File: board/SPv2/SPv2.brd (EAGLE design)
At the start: 63.8 x 22.9 mm, 33 parts, among them IC1 S34ML0XG1, IC2 F5508, IC4 74LS14D, Q1 12MHz

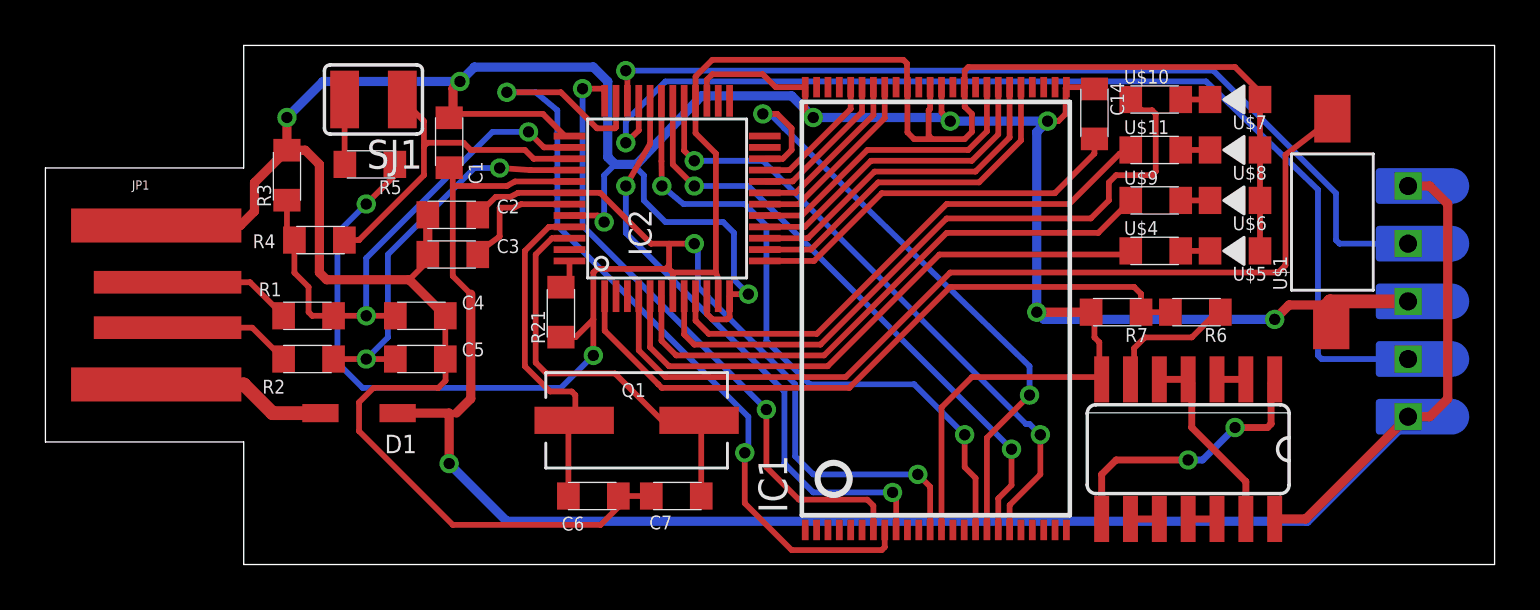
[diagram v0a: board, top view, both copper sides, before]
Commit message: added fiducals
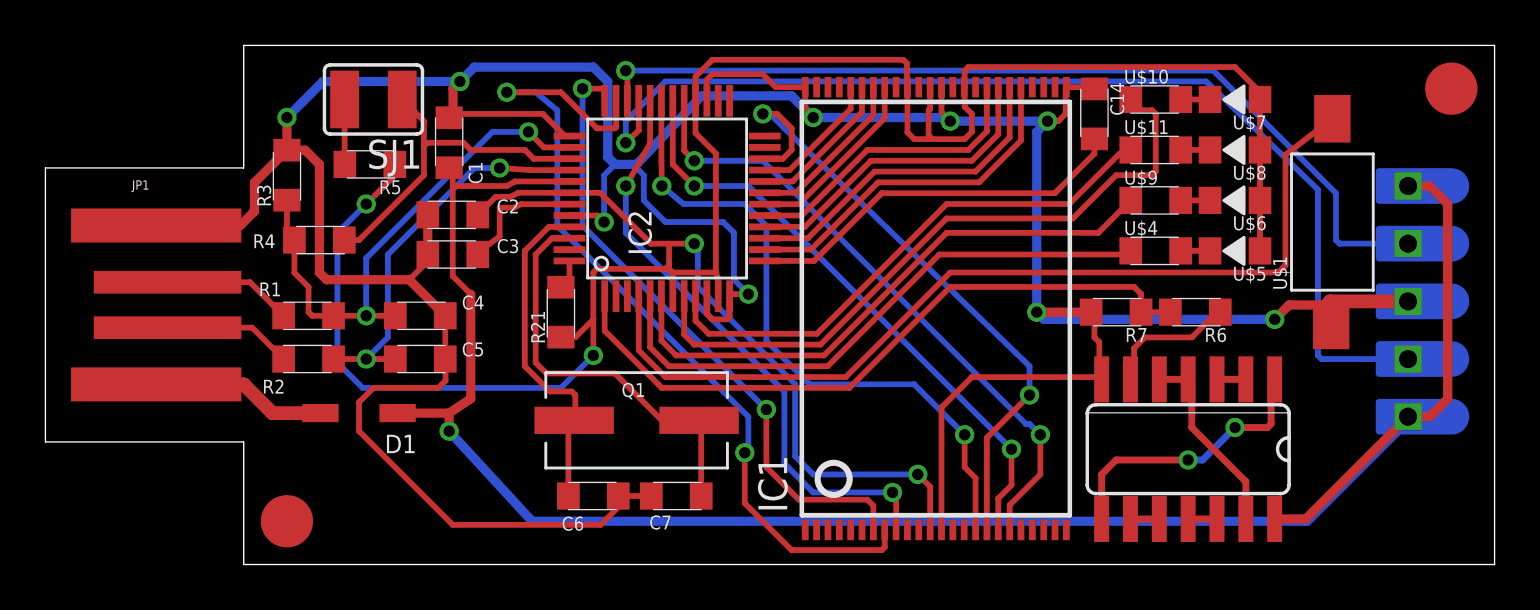
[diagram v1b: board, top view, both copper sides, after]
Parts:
- added U$12, U$3: FIDUCAL, Passives:FIDUCAL
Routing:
- net VBUS: track 87.3 -> 86.5 mm
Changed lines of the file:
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@@
 <grid distance="0.00625" unitdist="inch" unit="inch" style="lines" multiple="1" display="yes" altdistance="0.00625" altunitdist="inch" altunit="inch"/>
 <layers>
-<layer number="1" name="Top" color="4" fill="1" visible="no" active="yes"/>
+<layer number="1" name="Top" color="4" fill="1" visible="yes" active="yes"/>
 <layer number="2" name="Route2" color="1" fill="3" visible="no" active="no"/>
 <layer number="3" name="Route3" color="4" fill="3" visible="no" active="no"/>
@@
 <layer number="14" name="Route14" color="1" fill="6" visible="no" active="no"/>
 <layer number="15" name="Route15" color="4" fill="6" visible="no" active="no"/>
-<layer number="16" name="Bottom" color="1" fill="1" visible="no" active="yes"/>
-<layer number="17" name="Pads" color="2" fill="1" visible="no" active="yes"/>
-<layer number="18" name="Vias" color="2" fill="1" visible="no" active="yes"/>
+<layer number="16" name="Bottom" color="1" fill="1" visible="yes" active="yes"/>
+<layer number="17" name="Pads" color="2" fill="1" visible="yes" active="yes"/>
+<layer number="18" name="Vias" color="2" fill="1" visible="yes" active="yes"/>
 <layer number="19" name="Unrouted" color="6" fill="1" visible="yes" active="yes"/>
 <layer number="20" name="Dimension" color="15" fill="1" visible="yes" active="yes"/>
@@
 <element name="SJ1" library="jumper" package="SJW" value="" x="14.44625" y="20.47875" rot="R180"/>
 <element name="U$2" library="Passives" package="SNAP-HALF" value="SNAP-HALF" x="63.8175" y="11.58875" rot="MR180"/>
+<element name="U$3" library="Passives" package="FIDUCAL" value="FIDUCAL" x="10.63625" y="1.905"/>
+<element name="U$12" library="Passives" package="FIDUCAL" value="FIDUCAL" x="61.9125" y="20.955"/>
 </elements>
 <signals>
@@
 <wire x1="20.678765625" y1="16.868765625" x2="20.32" y2="16.66875" width="0.254" layer="1"/>
 <wire x1="15.51125" y1="6.6675" x2="17.78" y2="6.6675" width="0.4064" layer="1"/>
-<wire x1="17.78" y1="6.6675" x2="18.0975" y2="6.6675" width="0.254" layer="1"/>
 <wire x1="20.32" y1="16.66875" x2="17.93875" y2="16.66875" width="0.254" layer="1"/>
 <wire x1="17.93875" y1="16.66875" x2="17.93875" y2="12.7" width="0.254" layer="1"/>
 <wire x1="17.93875" y1="12.7" x2="18.7325" y2="11.90625" width="0.254" layer="1"/>
 <wire x1="18.7325" y1="11.90625" x2="18.7325" y2="7.3025" width="0.4064" layer="1"/>
-<wire x1="18.7325" y1="7.3025" x2="18.0975" y2="6.6675" width="0.4064" layer="1"/>
+<wire x1="18.7325" y1="7.3025" x2="17.78" y2="6.6675" width="0.4064" layer="1"/>
 <wire x1="17.78" y1="17.47375" x2="17.9275" y2="17.47375" width="0.254" layer="1"/>
 <wire x1="17.9275" y1="17.47375" x2="17.93875" y2="17.4625" width="0.254" layer="1"/>
@@
 <wire x1="60.0075" y1="6.50875" x2="60.0075" y2="6.35" width="0.4064" layer="16"/>
 <wire x1="60.0075" y1="6.35" x2="55.5625" y2="1.905" width="0.4064" layer="16"/>
-<wire x1="55.5625" y1="1.905" x2="20.32" y2="1.905" width="0.4064" layer="16"/>
-<wire x1="20.32" y1="1.905" x2="17.78" y2="4.445" width="0.4064" layer="16"/>
-<via x="17.78" y="4.445" extent="1-16" drill="0.5"/>
-<wire x1="17.78" y1="4.445" x2="17.78" y2="6.6675" width="0.4064" layer="1"/>
+<wire x1="55.5625" y1="1.905" x2="21.43125" y2="1.905" width="0.4064" layer="16"/>
+<wire x1="21.43125" y1="1.905" x2="17.78" y2="5.87375" width="0.4064" layer="16"/>
+<via x="17.78" y="5.87375" extent="1-16" drill="0.5"/>
+<wire x1="17.78" y1="5.87375" x2="17.78" y2="6.6675" width="0.4064" layer="1"/>
 <wire x1="54.13375" y1="2.0066" x2="55.50535" y2="2.0066" width="0.4064" layer="1"/>
 <wire x1="55.50535" y1="2.0066" x2="60.0075" y2="6.50875" width="0.4064" layer="1"/>
@@
 <wire x1="28.575" y1="9.68375" x2="34.13125" y2="9.68375" width="0.254" layer="1"/>
 <wire x1="34.13125" y1="9.68375" x2="39.6875" y2="15.24" width="0.254" layer="1"/>
-<wire x1="39.6875" y1="15.24" x2="46.0375" y2="15.24" width="0.254" layer="1"/>
-<wire x1="46.0375" y1="15.24" x2="46.83125" y2="16.03375" width="0.254" layer="1"/>
-<wire x1="46.83125" y1="16.03375" x2="46.83125" y2="16.8275" width="0.254" layer="1"/>
-<wire x1="46.83125" y1="16.8275" x2="47.14875" y2="17.145" width="0.254" layer="1"/>
+<wire x1="39.6875" y1="15.24" x2="45.24375" y2="15.24" width="0.254" layer="1"/>
+<wire x1="45.24375" y1="15.24" x2="47.14875" y2="17.145" width="0.254" layer="1"/>
 <wire x1="47.14875" y1="17.145" x2="48.73625" y2="17.145" width="0.254" layer="1"/>
 <wire x1="48.73625" y1="17.145" x2="48.895" y2="17.30375" width="0.254" layer="1"/>
